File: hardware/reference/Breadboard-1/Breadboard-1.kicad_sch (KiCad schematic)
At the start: 58 parts, among them J1 Left, J2 Right, J3 ICSP, J4 TTL Serial, Q31 HSM0903, Q32 HSM0903, Q41 2N7002, Q42 2N7002, Q43 2N7002, U11 AMS1117-5.0, U21 PIC18F06Q40-x/SS

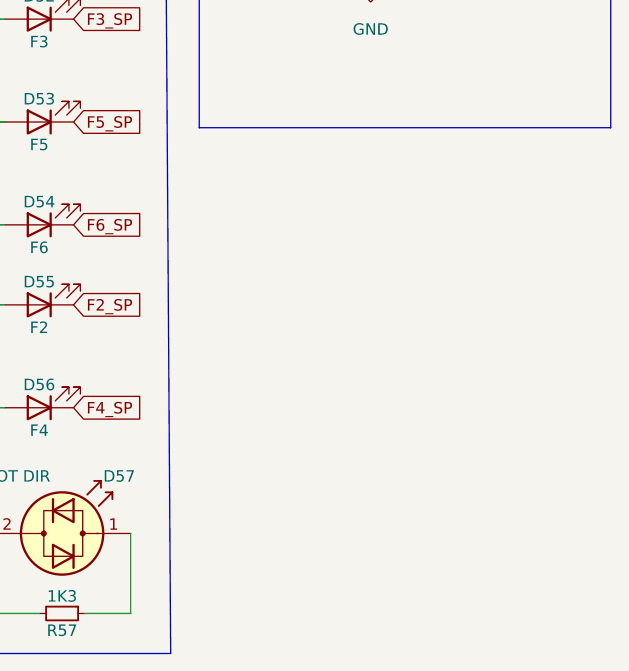
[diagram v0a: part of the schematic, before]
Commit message: Added a 100 Ohm load to enable readback when no motor is connected.
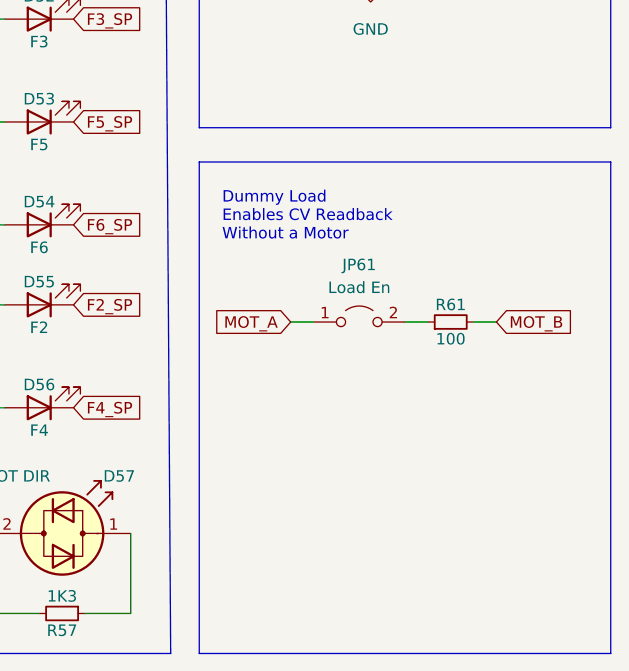
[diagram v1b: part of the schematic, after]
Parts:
- added JP61: Load En, Connector_PinHeader_2.54mm:PinHeader_1x02_P2.54mm_Vertical, symbol Jumper:Jumper_2_Open
- added R61: 100, Resistor_SMD:R_2512_6332Metric, symbol Device:R_Small
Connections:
- net MOT_A: now also JP61.1 (A)
- net MOT_B: now also R61.2
- new net: JP61.2 (B), R61.1
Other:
- note added: "Dummy Load Enables CV Readback Without a Motor"
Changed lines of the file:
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@@
+    (stroke (width 0) (type default) (color 0 0 0 0))
+  )
+  (wire (pts (xy 237.49 127) (xy 240.03 127))
     (stroke (width 0) (type default) (color 0 0 0 0))
   )
@@
     (stroke (width 0) (type default) (color 0 0 0 0))
   )
+  (polyline (pts (xy 227.33 109.22) (xy 273.05 109.22))
+    (stroke (width 0) (type default) (color 0 0 0 0))
+  )
   (wire (pts (xy 170.18 83.82) (xy 172.72 83.82))
     (stroke (width 0) (type default) (color 0 0 0 0))
@@
     (stroke (width 0) (type default) (color 0 0 0 0))
   )
+  (polyline (pts (xy 227.33 109.22) (xy 227.33 163.83))
+    (stroke (width 0) (type default) (color 0 0 0 0))
+  )
   (wire (pts (xy 69.85 73.66) (xy 73.66 73.66))
     (stroke (width 0) (type default) (color 0 0 0 0))
@@
     (stroke (width 0) (type default) (color 0 0 0 0))
   )
+  (wire (pts (xy 257.81 127) (xy 260.35 127))
+    (stroke (width 0) (type default) (color 0 0 0 0))
+  )
   (wire (pts (xy 134.62 83.82) (xy 137.16 83.82))
     (stroke (width 0) (type default) (color 0 0 0 0))
@@
     (stroke (width 0) (type default) (color 0 0 0 0))
   )
+  (polyline (pts (xy 227.33 163.83) (xy 273.05 163.83))
+    (stroke (width 0) (type default) (color 0 0 0 0))
+  )
   (wire (pts (xy 204.47 104.775) (xy 205.74 104.775))
     (stroke (width 0) (type default) (color 0 0 0 0))
@@
     (stroke (width 0) (type default) (color 0 0 0 0))
   )
+  (polyline (pts (xy 273.05 109.22) (xy 273.05 163.83))
+    (stroke (width 0) (type default) (color 0 0 0 0))
+  )
   (wire (pts (xy 250.19 33.02) (xy 250.19 39.37))
     (stroke (width 0) (type default) (color 0 0 0 0))
@@
   )
   (wire (pts (xy 171.45 30.48) (xy 179.07 30.48))
+    (stroke (width 0) (type default) (color 0 0 0 0))
+  )
+  (wire (pts (xy 250.19 127) (xy 252.73 127))
     (stroke (width 0) (type default) (color 0 0 0 0))
   )
@@
     (effects (font (size 1.27 1.27)) (justify left bottom))
   )
+  (text "Dummy Load\nEnables CV Readback\nWithout a Motor" (at 229.87 118.11 0)
+    (effects (font (size 1.27 1.27)) (justify left bottom))
+  )
   (text "Functions F0F/F0R are \ndirect drive." (at 123.19 76.2 0)
     (effects (font (size 1.27 1.27)) (justify left bottom))
@@
     )
   )
+  (global_label "MOT_A" (shape input) (at 237.49 127 180) (fields_autoplaced)
+    (effects (font (size 1.27 1.27)) (justify right))
+    (property "Intersheet References" "${INTERSHEET_REFS}" (id 0) (at 229.2712 126.9206 0)
+      (effects (font (size 1.27 1.27)) (justify right) hide)
+    )
+  )
   (global_label "F4" (shape input) (at 99.06 99.06 0) (fields_autoplaced)
     (effects (font (size 1.27 1.27)) (justify left))
@@
     (effects (font (size 1.27 1.27)) (justify left))
     (property "Intersheet References" "${INTERSHEET_REFS}" (id 0) (at 221.5183 83.1056 0)
+      (effects (font (size 1.27 1.27)) (justify left) hide)
+    )
+  )
+  (global_label "MOT_B" (shape input) (at 260.35 127 0) (fields_autoplaced)
+    (effects (font (size 1.27 1.27)) (justify left))
+    (property "Intersheet References" "${INTERSHEET_REFS}" (id 0) (at 268.7502 126.9206 0)
       (effects (font (size 1.27 1.27)) (justify left) hide)
     )
@@
     )
     (property "Specification" "SOD-523, 50V, 1A Schottky barrier rectifier diode" (id 4) (at 38.1 36.83 0)
+      (effects (font (size 1.27 1.27)) hide)
+    )
+    (pin "1")
+    (pin "2")
+  )
+  (symbol (lib_id "Device:R_Small") (at 255.27 127 90) (unit 1)
+    (in_bom yes) (on_board yes)
+    (property "Reference" "R61" (id 0) (at 255.27 125.095 90))
+    (property "Value" "100" (id 1) (at 255.27 128.905 90))
+    (property "Footprint" "Resistor_SMD:R_2512_6332Metric" (id 2) (at 255.27 127 0)
+      (effects (font (size 1.27 1.27)) hide)
+    )
+    (property "Datasheet" "Generic Passive" (id 3) (at 255.27 127 0)
+      (effects (font (size 1.27 1.27)) hide)
+    )
+    (property "Specification" "2512 100 Ω 5% 2W" (id 4) (at 255.27 127 0)
       (effects (font (size 1.27 1.27)) hide)
     )
@@
     (pin "2")
   )
+  (symbol (lib_id "Jumper:Jumper_2_Open") (at 245.11 127 0) (unit 1)
+    (in_bom yes) (on_board yes) (fields_autoplaced)
+    (property "Reference" "JP61" (id 0) (at 245.11 120.65 0))
+    (property "Value" "Load En" (id 1) (at 245.11 123.19 0))
+    (property "Footprint" "Connector_PinHeader_2.54mm:PinHeader_1x02_P2.54mm_Vertical" (id 2) (at 245.11 127 0)
+      (effects (font (size 1.27 1.27)) hide)
+    )
+    (property "Datasheet" "~" (id 3) (at 245.11 127 0)
+      (effects (font (size 1.27 1.27)) hide)
+    )
+    (pin "1")
+    (pin "2")
+  )
   (symbol (lib_id "Leo's Library:TPC8408") (at 138.938 39.37 0) (unit 1)
     (in_bom yes) (on_board yes)
@@
       (reference "J4") (unit 1) (value "TTL Serial") (footprint "Connector_PinSocket_2.54mm:PinSocket_1x05_P2.54mm_Vertical")
     )
+    (path "/695d937f-802a-48dc-821f-174b87bac671"
+      (reference "JP61") (unit 1) (value "Load En") (footprint "Connector_PinHeader_2.54mm:PinHeader_1x02_P2.54mm_Vertical")
+    )
     (path "/6a3ac14c-4a85-4667-966a-7d0148472c12"
       (reference "Q31") (unit 1) (value "HSM0903") (footprint "Package_SO:SOP-8_3.9x4.9mm_P1.27mm")
@@
       (reference "R57") (unit 1) (value "1K3") (footprint "Resistor_SMD:R_0402_1005Metric")
     )
+    (path "/18c75862-c5fb-4ab2-8303-dcda4de82b09"
+      (reference "R61") (unit 1) (value "100") (footprint "Resistor_SMD:R_2512_6332Metric")
+    )
     (path "/3840e91e-0efb-47a3-bd0e-13b143df20fb"

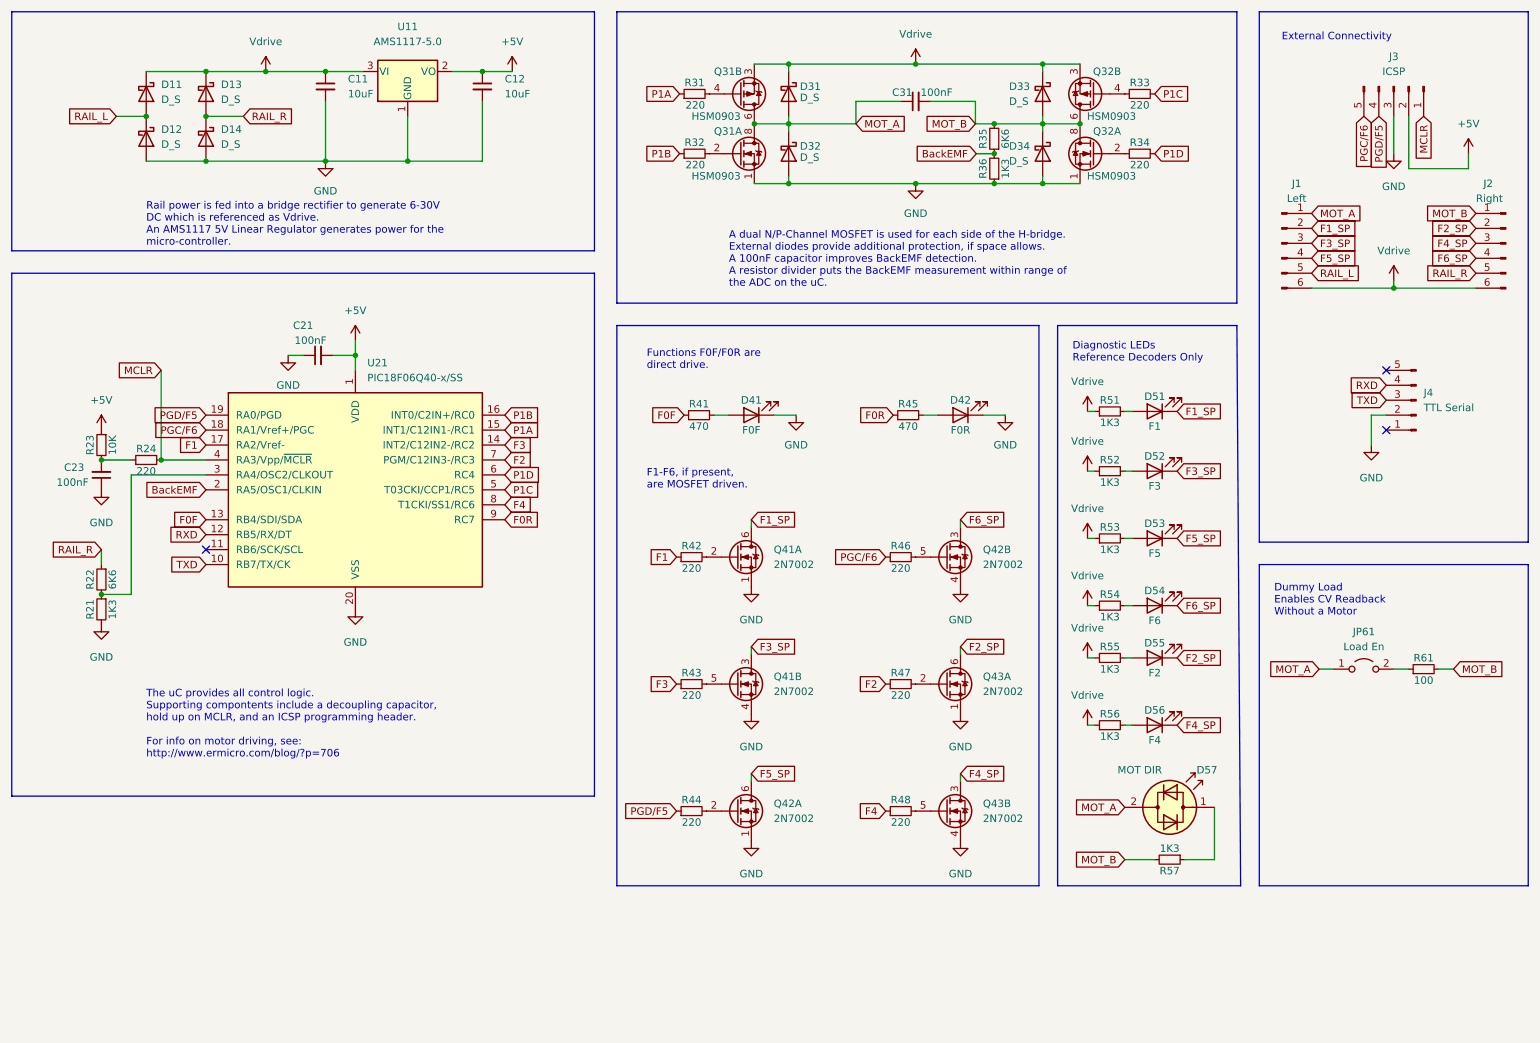
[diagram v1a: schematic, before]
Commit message: Add pre-biased transistors to drive high side.  Update LED part to more common.
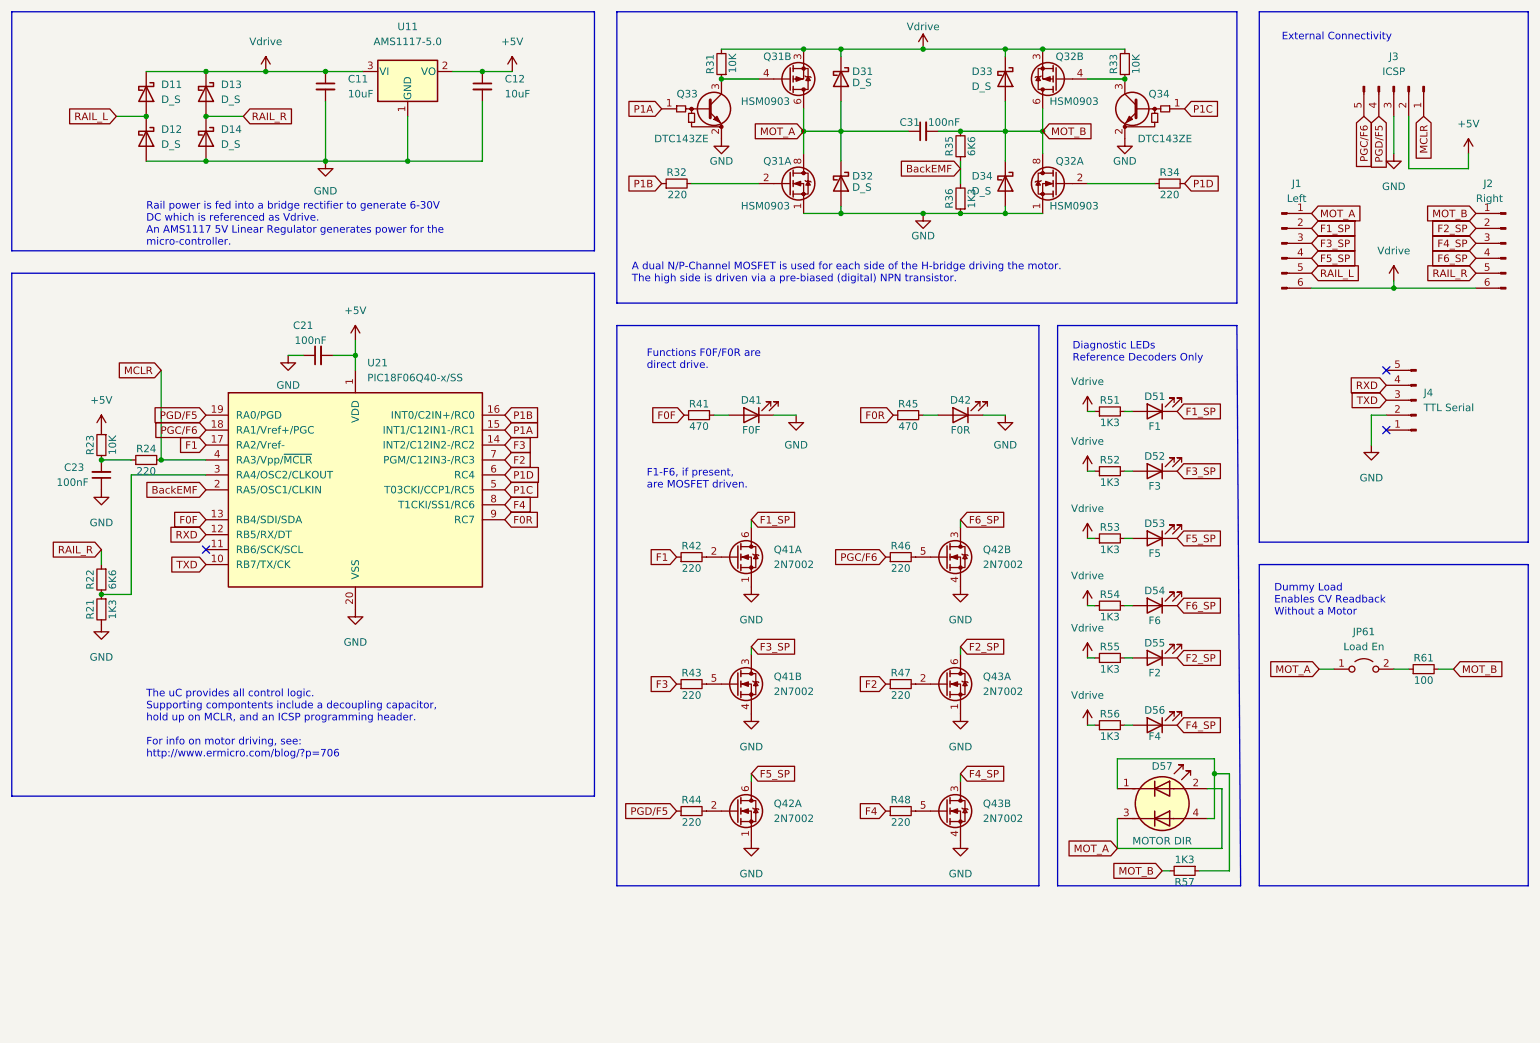
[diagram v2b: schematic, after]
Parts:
- removed D57: MOT DIR, LED_SMD:LED_0805_2012Metric, symbol Device:LED_Dual_Bidirectional
- added D57: MOTOR DIR, LED_SMD:LED_RGB_1210, symbol Device:LED_Dual_KAKA
- added Q33, Q34: DTC143ZE, Package_TO_SOT_SMD:SOT-523, symbol Device:Q_NPN_BEC_BRT
- D11, D12, D13, D14: footprint Diode_SMD:D_SOD-128 -> Diode_SMD:D_SOD-523
- R31, R33: value 220 -> 10K; Specification 0402 220 Ω 1% 1/8W -> 0402 10K Ω 1% 1/8W
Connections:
- net GND: now also Q33.2 (E), Q34.2 (E)
- net MOT_A: now also D57.2 (K1), D57.3 (A2)
- net P1A: now also Q33.1 (B); no longer R31.1
- net P1C: now also Q34.1 (B); no longer R33.2
- net Vdrive: now also R31.2, R33.2
- net at R57.1: now also D57.1 (A1), D57.4 (K2)
- net at Q32.4 (G), R33.1: now also Q34.3 (C)
- net at Q31.4 (G): now also R31.1, Q33.3 (C); no longer R31.2
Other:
- note added: "A dual N/P-Channel MOSFET is used for each side of the H-bridge driving the motor. The high side is driven via a pre-biased (digital) NPN transistor."
- note removed: "A dual N/P-Channel MOSFET is used for each side of the H-bridge. External diodes provide additional protection, if space allows. A 100nF capacitor improves BackEMF detection. A resistor divider puts the BackEMF measurement within range of the ADC on the uC."
- moved on the sheet: C31, D31, D32, D33, D34, Q31A, Q31B, Q32A, Q32B, R31, R32, R33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
